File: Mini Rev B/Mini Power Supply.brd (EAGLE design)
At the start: 52.1 x 36.8 mm, 20 parts, among them J1 POWER_JACKPTH

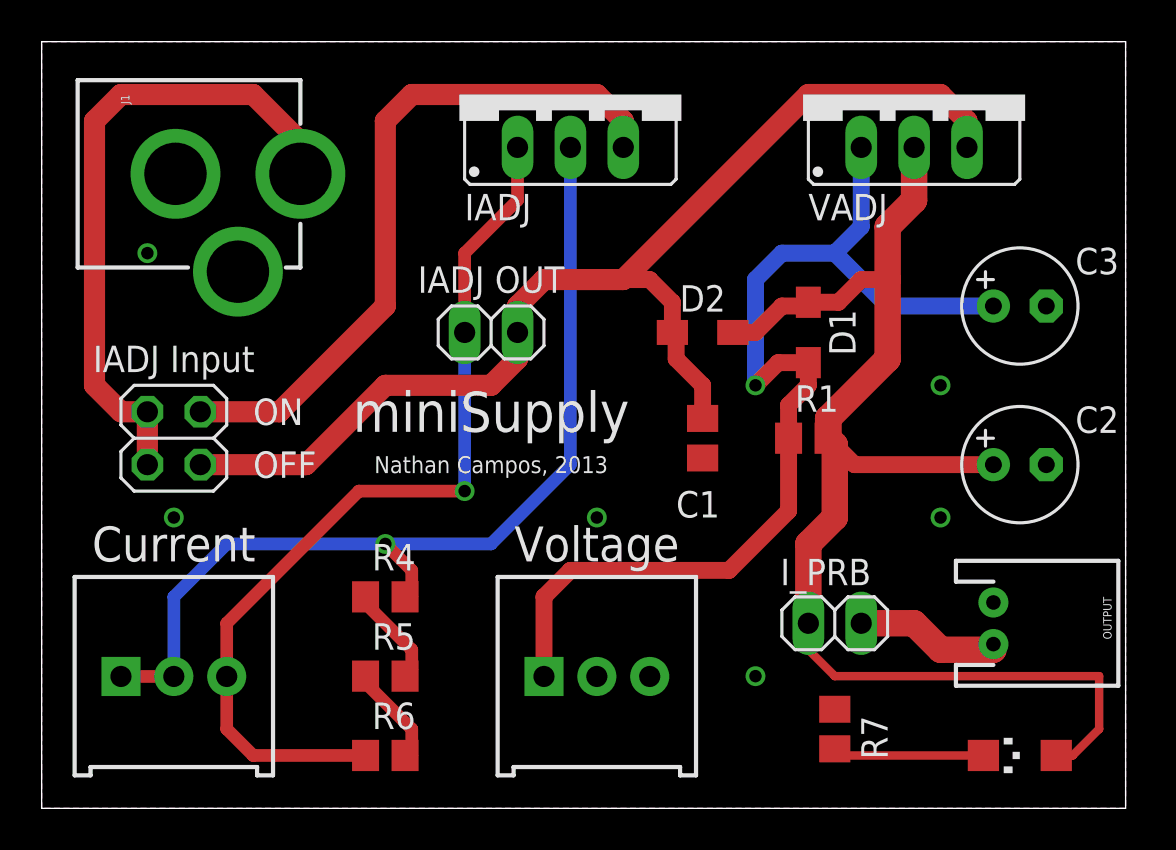
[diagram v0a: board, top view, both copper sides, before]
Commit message: Changed the input to a JST and connected the ON LED to VCC
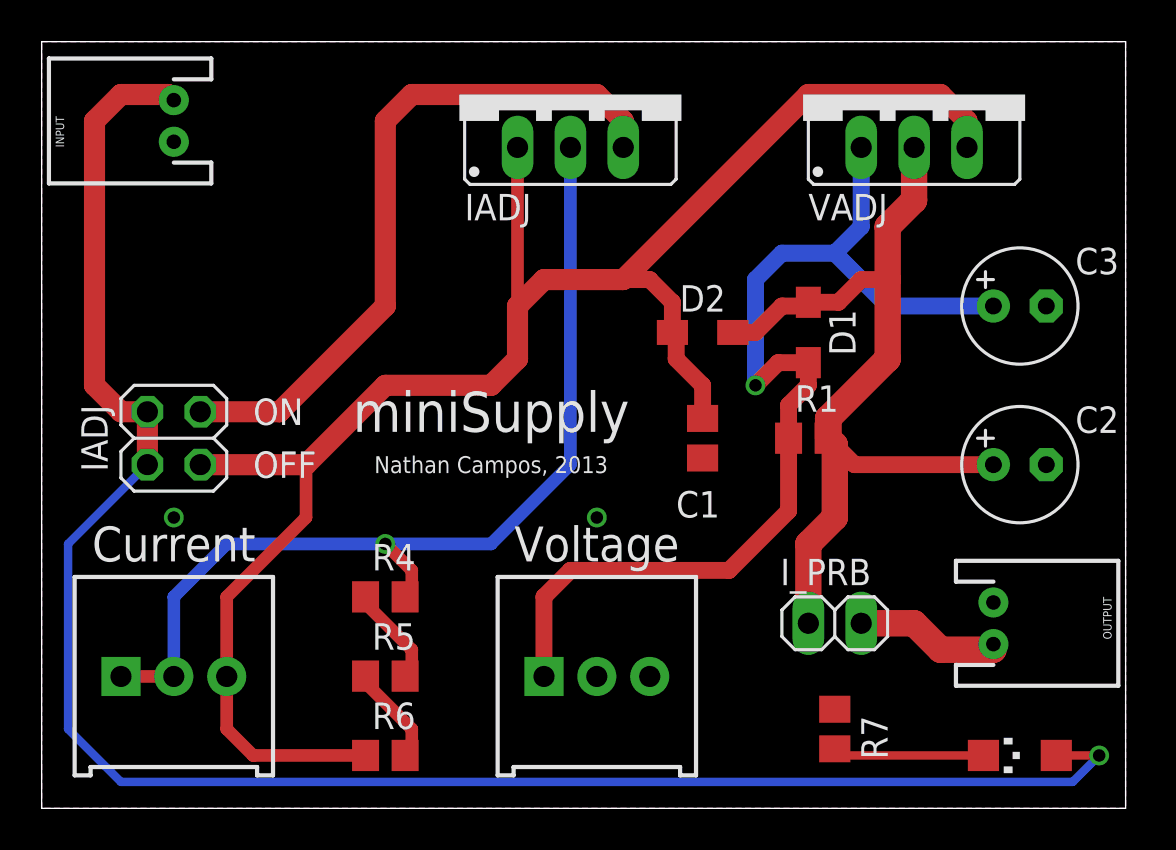
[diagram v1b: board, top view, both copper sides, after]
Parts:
- removed IADJ_SEL: (no value), pinhead:1X02
- removed J1: POWER_JACKPTH, SparkFun-Connectors:POWER_JACK_PTH
- added INPUT: M02JST-PTH-2, SparkFun-Connectors:JST-2-PTH
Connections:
- removed net N$4: IADJ.1, IADJ_SEL.1, R3.3, R6.1
- net GND: now also INPUT.1; no longer J1.GND, J1.GNDBREAK
- net VADJ_IN: now also IADJ.1, R3.3, R6.1; no longer IADJ_SEL.2
- net VCC: now also INPUT.2, ON.A; no longer J1.PWR
- net VOUT: no longer ON.A
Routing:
- net VCC: track 31.2 -> 90.2 mm, vias 0 -> 1
- net N$4: track 43.9 -> 0.00 mm, vias 1 -> 0
- net VADJ_IN: track 56.5 -> 85.6 mm
- net VOUT: track 63.1 -> 42.2 mm
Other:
- board text added: "IADJ"
- board text removed: "IADJ Input"
- board text removed: "IADJ OUT"
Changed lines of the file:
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@@
 <text x="6.35" y="12.7" size="1.6764" layer="21" align="center">Current</text>
 <text x="26.67" y="12.7" size="1.6764" layer="21" align="center">Voltage</text>
-<text x="21.59" y="25.4" size="1.27" layer="21" align="center">IADJ OUT</text>
-<text x="6.35" y="21.59" size="1.27" layer="21" align="center">IADJ Input</text>
+<text x="2.54" y="17.78" size="1.27" layer="21" rot="R90" align="center">IADJ</text>
 <text x="10.16" y="19.05" size="1.27" layer="21" align="center-left">ON</text>
 <text x="10.16" y="16.51" size="1.27" layer="21" align="center-left">OFF</text>
 <text x="21.59" y="19.05" size="1.9304" layer="21" align="center">miniSupply</text>
 <text x="21.59" y="16.51" size="0.8128" layer="21" align="center">Nathan Campos, 2013</text>
-<text x="50.8" y="34.29" size="0.8128" layer="22" rot="MR270" align="center">Rev B</text>
+<text x="50.8" y="33.02" size="1.27" layer="22" rot="MR270" align="center">Rev B</text>
 </plain>
 <attributes>
@@
 <element name="R5" library="rcl" package="R0805" value="100Ω" x="16.51" y="6.35"/>
 <element name="R6" library="rcl" package="R0805" value="100Ω" x="16.51" y="2.54"/>
-<element name="IADJ_SEL" library="pinhead" package="1X02" value="" x="21.59" y="22.86" smashed="yes">
-<attribute name="VALUE" x="19.05" y="19.685" size="1.27" layer="27"/>
-</element>
 <element name="ON" library="led" package="CHIPLED_1206" value="" x="46.99" y="2.54" smashed="yes" rot="R90">
 <attribute name="VALUE" x="48.26" y="5.08" size="1.27" layer="27" rot="R180"/>
@@
 <element name="R7" library="rcl" package="R0805" value="1kΩ" x="38.1" y="3.81" rot="R270"/>
 <element name="I_PRB" library="pinhead" package="1X02" value="" x="38.1" y="8.89"/>
-<element name="J1" library="SparkFun-Connectors" package="POWER_JACK_PTH" value="POWER_JACKPTH" x="-1.27" y="30.48" rot="R270"/>
 <element name="OUTPUT" library="SparkFun-Connectors" package="JST-2-PTH" value="M02JST-PTH-2" x="45.72" y="8.89" rot="R270"/>
+<element name="INPUT" library="SparkFun-Connectors" package="JST-2-PTH" value="M02JST-PTH-2" x="6.35" y="33.02" rot="R90"/>
 </elements>
 <signals>
@@
 <contactref element="D2" pad="A"/>
 <contactref element="D1" pad="C"/>
-<contactref element="ON" pad="A"/>
 <contactref element="I_PRB" pad="1"/>
-<wire x1="48.74" y1="2.54" x2="49.53" y2="2.54" width="0.4064" layer="1"/>
-<wire x1="49.53" y1="2.54" x2="50.8" y2="3.81" width="0.4064" layer="1"/>
-<wire x1="50.8" y1="3.81" x2="50.8" y2="6.35" width="0.4064" layer="1"/>
-<wire x1="50.8" y1="6.35" x2="38.1" y2="6.35" width="0.4064" layer="1"/>
-<wire x1="38.1" y1="6.35" x2="36.83" y2="7.62" width="0.4064" layer="1"/>
-<wire x1="36.83" y1="7.62" x2="36.83" y2="8.89" width="0.4064" layer="1"/>
 <wire x1="33.2" y1="22.86" x2="34.29" y2="22.86" width="0.8128" layer="1"/>
 <wire x1="34.29" y1="22.86" x2="35.56" y2="24.13" width="0.8128" layer="1"/>
@@
 <contactref element="VIN_SEL" pad="3"/>
 <contactref element="VIN_SEL" pad="1"/>
-<contactref element="J1" pad="PWR"/>
-<wire x1="12.43" y1="30.48" x2="12.43" y2="32.02" width="1.016" layer="1"/>
-<wire x1="12.43" y1="32.02" x2="10.16" y2="34.29" width="1.016" layer="1"/>
-<wire x1="10.16" y1="34.29" x2="3.81" y2="34.29" width="1.016" layer="1"/>
-<wire x1="3.81" y1="34.29" x2="2.54" y2="33.02" width="1.016" layer="1"/>
-<wire x1="2.54" y1="33.02" x2="2.54" y2="20.32" width="1.016" layer="1"/>
-<wire x1="2.54" y1="20.32" x2="3.81" y2="19.05" width="1.016" layer="1"/>
-<wire x1="3.81" y1="19.05" x2="5.08" y2="19.05" width="1.016" layer="1"/>
 <wire x1="5.08" y1="19.05" x2="5.08" y2="16.51" width="1.016" layer="1"/>
+<contactref element="INPUT" pad="2"/>
+<contactref element="ON" pad="A"/>
+<wire x1="48.74" y1="2.54" x2="50.8" y2="2.54" width="0.4064" layer="1"/>
+<wire x1="5.08" y1="16.51" x2="1.27" y2="12.7" width="0.4064" layer="16"/>
+<wire x1="1.27" y1="12.7" x2="1.27" y2="3.81" width="0.4064" layer="16"/>
+<wire x1="1.27" y1="3.81" x2="3.81" y2="1.27" width="0.4064" layer="16"/>
+<wire x1="3.81" y1="1.27" x2="49.53" y2="1.27" width="0.4064" layer="16"/>
+<wire x1="49.53" y1="1.27" x2="50.8" y2="2.54" width="0.4064" layer="16"/>
+<wire x1="5.08" y1="19.05" x2="3.81" y2="19.05" width="1.016" layer="1"/>
+<wire x1="3.81" y1="19.05" x2="2.54" y2="20.32" width="1.016" layer="1"/>
+<wire x1="2.54" y1="20.32" x2="2.54" y2="33.02" width="1.016" layer="1"/>
+<wire x1="2.54" y1="33.02" x2="3.81" y2="34.29" width="1.016" layer="1"/>
+<wire x1="3.81" y1="34.29" x2="6.08" y2="34.29" width="1.016" layer="1"/>
+<wire x1="6.08" y1="34.29" x2="6.35" y2="34.02" width="1.016" layer="1"/>
+<via x="50.8" y="2.54" extent="1-16" drill="0.6"/>
 </signal>
 <signal name="GND">
@@
 <contactref element="C2" pad="-"/>
 <contactref element="R7" pad="1"/>
-<contactref element="J1" pad="GNDBREAK"/>
-<contactref element="J1" pad="GND"/>
 <contactref element="OUTPUT" pad="1"/>
 <polygon width="0.4064" layer="16" isolate="0.3048">
@@
 <vertex x="0" y="0"/>
 </polygon>
-<via x="5.08" y="26.67" extent="1-16" drill="0.6" shape="octagon"/>
 <via x="6.35" y="13.97" extent="1-16" drill="0.6" shape="octagon"/>
 <via x="26.67" y="13.97" extent="1-16" drill="0.6" shape="octagon"/>
-<via x="34.29" y="6.35" extent="1-16" drill="0.6" shape="octagon"/>
-<via x="43.18" y="13.97" extent="1-16" drill="0.6" shape="octagon"/>
-<via x="43.18" y="20.32" extent="1-16" drill="0.6" shape="octagon"/>
+<contactref element="INPUT" pad="1"/>
 </signal>
 <signal name="VADJ_IN">
@@
 <contactref element="D2" pad="C"/>
 <contactref element="VIN_SEL" pad="4"/>
-<contactref element="IADJ_SEL" pad="2"/>
 <wire x1="7.62" y1="16.51" x2="12.7" y2="16.51" width="1.016" layer="1"/>
 <wire x1="12.7" y1="16.51" x2="16.51" y2="20.32" width="1.016" layer="1"/>
 <wire x1="16.51" y1="20.32" x2="21.59" y2="20.32" width="1.016" layer="1"/>
 <wire x1="21.59" y1="20.32" x2="22.86" y2="21.59" width="1.016" layer="1"/>
-<wire x1="22.86" y1="21.59" x2="22.86" y2="22.86" width="1.016" layer="1"/>
-<wire x1="22.86" y1="22.86" x2="22.86" y2="24.13" width="1.016" layer="1"/>
 <wire x1="22.86" y1="24.13" x2="24.13" y2="25.4" width="1.016" layer="1"/>
 <wire x1="24.13" y1="25.4" x2="27.94" y2="25.4" width="1.016" layer="1"/>
@@
 <wire x1="30.3" y1="24.31" x2="29.21" y2="25.4" width="0.8128" layer="1"/>
 <wire x1="29.21" y1="25.4" x2="27.94" y2="25.4" width="0.8128" layer="1"/>
+<contactref element="IADJ" pad="1"/>
+<contactref element="R3" pad="3"/>
+<contactref element="R6" pad="1"/>
+<wire x1="8.89" y1="6.335" x2="8.89" y2="3.81" width="0.6096" layer="1"/>
+<wire x1="8.89" y1="3.81" x2="10.16" y2="2.54" width="0.6096" layer="1"/>
+<wire x1="10.16" y1="2.54" x2="15.56" y2="2.54" width="0.6096" layer="1"/>
+<wire x1="8.89" y1="6.335" x2="8.89" y2="10.16" width="0.6096" layer="1"/>
+<wire x1="8.89" y1="10.16" x2="12.7" y2="13.97" width="0.6096" layer="1"/>
+<wire x1="12.7" y1="13.97" x2="12.7" y2="16.51" width="0.6096" layer="1"/>
+<wire x1="22.86" y1="21.59" x2="22.86" y2="24.13" width="1.016" layer="1"/>
+<wire x1="22.86" y1="31.75" x2="22.86" y2="24.13" width="0.6096" layer="1"/>
 </signal>
 <signal name="IADJ_IN">
@@
 <wire x1="25.4" y1="16.51" x2="25.4" y2="31.75" width="0.6096" layer="16"/>
 </signal>
-<signal name="N$4">
-<contactref element="IADJ" pad="1"/>
-<contactref element="R3" pad="3"/>
-<contactref element="R6" pad="1"/>
-<contactref element="IADJ_SEL" pad="1"/>
-<wire x1="8.89" y1="6.335" x2="8.89" y2="3.81" width="0.6096" layer="1"/>
-<wire x1="8.89" y1="3.81" x2="10.16" y2="2.54" width="0.6096" layer="1"/>
-<wire x1="10.16" y1="2.54" x2="15.56" y2="2.54" width="0.6096" layer="1"/>
-<wire x1="8.89" y1="6.335" x2="8.89" y2="8.89" width="0.6096" layer="1"/>
-<wire x1="8.89" y1="8.89" x2="15.24" y2="15.24" width="0.6096" layer="1"/>
-<wire x1="15.24" y1="15.24" x2="20.32" y2="15.24" width="0.6096" layer="1"/>
-<wire x1="22.86" y1="31.75" x2="22.86" y2="29.21" width="0.6096" layer="1"/>
-<wire x1="22.86" y1="29.21" x2="20.32" y2="26.67" width="0.6096" layer="1"/>
-<wire x1="20.32" y1="26.67" x2="20.32" y2="22.86" width="0.6096" layer="1"/>
-<via x="20.32" y="15.24" extent="1-16" drill="0.6"/>
-<wire x1="20.32" y1="15.24" x2="20.32" y2="22.86" width="0.6096" layer="16"/>
-</signal>
 <signal name="N$2">

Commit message: Finished most of the new revision
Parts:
- added Q1: BC817-25LT1SMD, transistor-npn:SOT23-BEC
- added R8: 1kΩ, rcl:R0805
- added U$1: 9V, dicons:ICON_BATTERY-S
- moved C3 8.89 mm to (47.0, 33.0)
- moved C2 8.89 mm to (47.0, 25.4)
- moved IADJ 7.73 mm to (17.8, 35.6)
- moved VADJ 7.73 mm to (34.3, 35.6)
- moved OUTPUT 7.62 mm to (45.7, 16.5)
- moved ON 7.62 mm to (47.0, 10.2)
- moved I_PRB 1.80 mm to (39.4, 10.2)
- moved C1 1.27 mm to (31.8, 19.1)
- moved D1 1.27 mm to (36.8, 24.1)
- moved D2 1.27 mm to (31.8, 24.1)
- moved R1 1.27 mm to (36.8, 19.1)
- turned R7 to 90 degrees
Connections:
- new net N$4: Q1.C, R7.1
- new net N$8: Q1.B, R8.2
- net GND: now also Q1.E; no longer R7.1
- net VOUT: now also R8.1
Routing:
- net VOUT: track 42.2 -> 61.5 mm
- net N$8: track 0.00 -> 16.7 mm
- net N$4: track 0.00 -> 10.5 mm
- net N$3: track 51.5 -> 59.8 mm
- net VCC: track 90.2 -> 97.4 mm
- net N$1: track 46.7 -> 41.8 mm
- net IADJ_IN: track 33.6 -> 29.5 mm
- net N$6: track 7.27 -> 10.9 mm
- net N$7: track 7.15 -> 9.53 mm
- net VADJ_IN: track 85.6 -> 83.4 mm

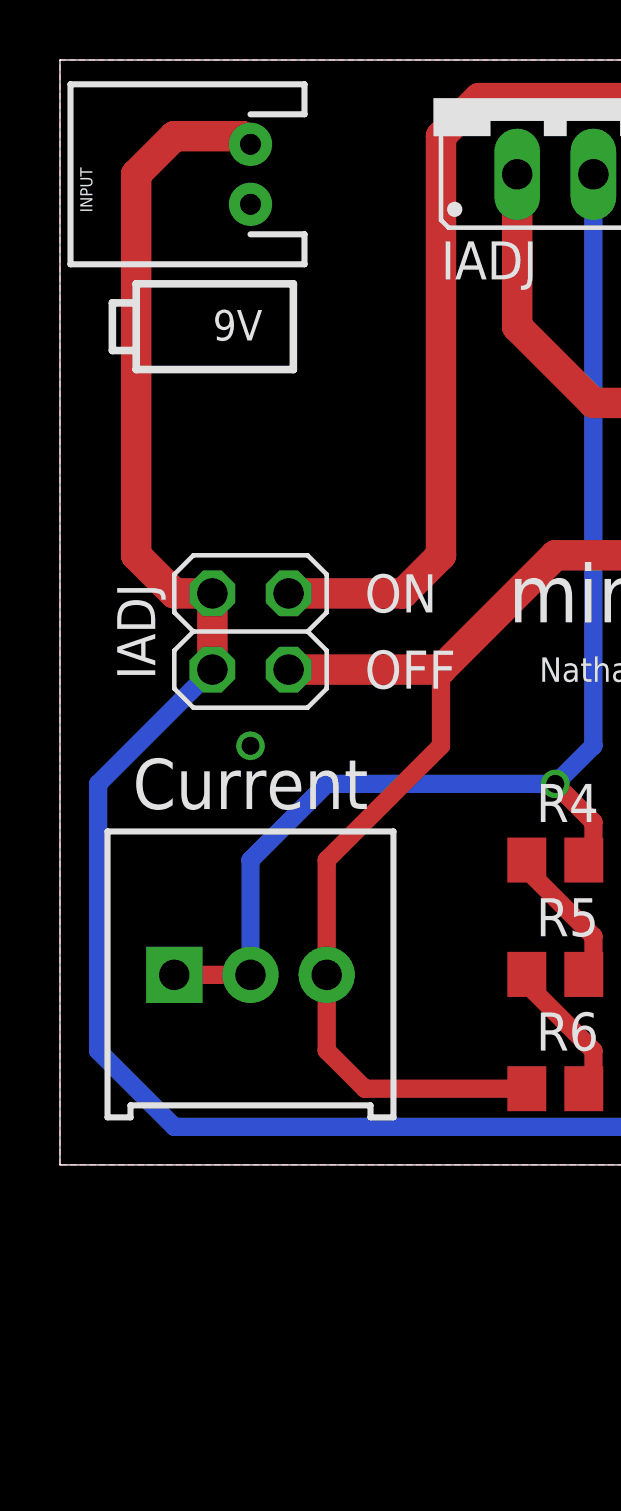
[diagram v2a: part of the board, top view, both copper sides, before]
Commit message: Started working on the negative rail for the mini Rev B
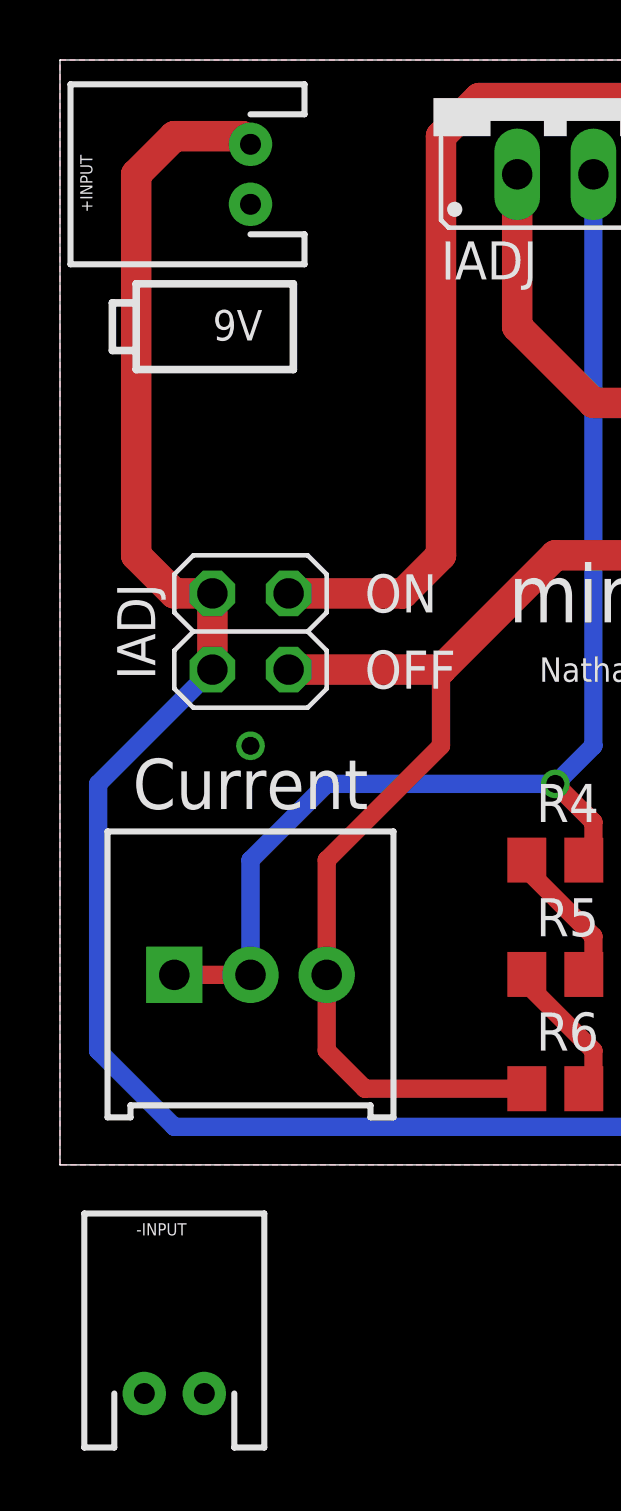
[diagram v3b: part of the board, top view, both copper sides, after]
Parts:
- added -INPUT: M02JST-PTH-2, SparkFun-Connectors:JST-2-PTH
- renumbered INPUT to +INPUT
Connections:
- new net V-: -INPUT.1
- net GND: now also -INPUT.2
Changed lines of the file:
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@@
 <element name="I_PRB" library="pinhead" package="1X02" value="" x="39.37" y="10.16"/>
 <element name="OUTPUT" library="SparkFun-Connectors" package="JST-2-PTH" value="M02JST-PTH-2" x="45.72" y="16.51" rot="R270"/>
-<element name="INPUT" library="SparkFun-Connectors" package="JST-2-PTH" value="M02JST-PTH-2" x="6.35" y="33.02" rot="R90"/>
+<element name="+INPUT" library="SparkFun-Connectors" package="JST-2-PTH" value="M02JST-PTH-2" x="6.35" y="33.02" rot="R90"/>
 <element name="U$1" library="dicons" package="ICON_BATTERY-S" value="9V" x="5.08" y="27.94" rot="R180"/>
 <element name="Q1" library="transistor-npn" package="SOT23-BEC" value="BC817-25LT1SMD" x="46.99" y="5.08" smashed="yes">
@@
 <attribute name="NAME" x="36.83" y="2.54" size="1.27" layer="25" rot="R90"/>
 </element>
+<element name="-INPUT" library="SparkFun-Connectors" package="JST-2-PTH" value="M02JST-PTH-2" x="3.81" y="-7.62"/>
 </elements>
 <signals>
@@
 <contactref element="VIN_SEL" pad="1"/>
 <wire x1="5.08" y1="19.05" x2="5.08" y2="16.51" width="1.016" layer="1"/>
-<contactref element="INPUT" pad="2"/>
+<contactref element="+INPUT" pad="2"/>
 <contactref element="ON" pad="A"/>
 <wire x1="5.08" y1="16.51" x2="1.27" y2="12.7" width="0.6096" layer="16"/>
@@
 <via x="6.35" y="13.97" extent="1-16" drill="0.6" shape="octagon"/>
 <via x="26.67" y="13.97" extent="1-16" drill="0.6" shape="octagon"/>
-<contactref element="INPUT" pad="1"/>
+<contactref element="+INPUT" pad="1"/>
 <contactref element="Q1" pad="E"/>
+<contactref element="-INPUT" pad="2"/>
+<wire x1="48.26" y1="25.4" x2="48.26" y2="33.02" width="0" layer="19" extent="1-1"/>
+<wire x1="45.72" y1="17.51" x2="48.26" y2="25.4" width="0" layer="19" extent="1-1"/>
+<wire x1="47.94" y1="3.98" x2="45.72" y2="17.51" width="0" layer="19" extent="1-1"/>
+<wire x1="31.75" y1="18.1" x2="45.72" y2="17.51" width="0" layer="19" extent="1-1"/>
+<wire x1="26.67" y1="13.97" x2="31.75" y2="18.1" width="0" layer="19" extent="1-1"/>
+<wire x1="26.67" y1="6.335" x2="26.67" y2="13.97" width="0" layer="19" extent="1-1"/>
+<wire x1="29.21" y1="6.335" x2="26.67" y2="6.335" width="0" layer="19" extent="1-1"/>
+<wire x1="6.35" y1="13.97" x2="26.67" y2="13.97" width="0" layer="19" extent="1-1"/>
+<wire x1="6.35" y1="32.02" x2="6.35" y2="13.97" width="0" layer="19" extent="1-1"/>
+<wire x1="4.81" y1="-7.62" x2="6.35" y2="13.97" width="0" layer="19" extent="1-1"/>
 </signal>
 <signal name="VADJ_IN">
@@
 <wire x1="34.61" y1="5.08" x2="34.29" y2="4.76" width="0.4064" layer="1"/>
 </signal>
+<signal name="V-">
+<contactref element="-INPUT" pad="1"/>
+</signal>
 </signals>
